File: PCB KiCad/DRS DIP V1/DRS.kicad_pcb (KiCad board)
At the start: 2 copper layers, 97.5 x 82.5 mm, 62 parts, among them J1 Jp7, J2 Jp8, J3 Jp8, J4 Conn_02x05_Odd_Even, SW1 SW_Push, SW2 SW_Push, SW3 SW_Push, U1 ATmega8-16PU, U2 LM2596S-ADJ, U3 LM2596S-ADJ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

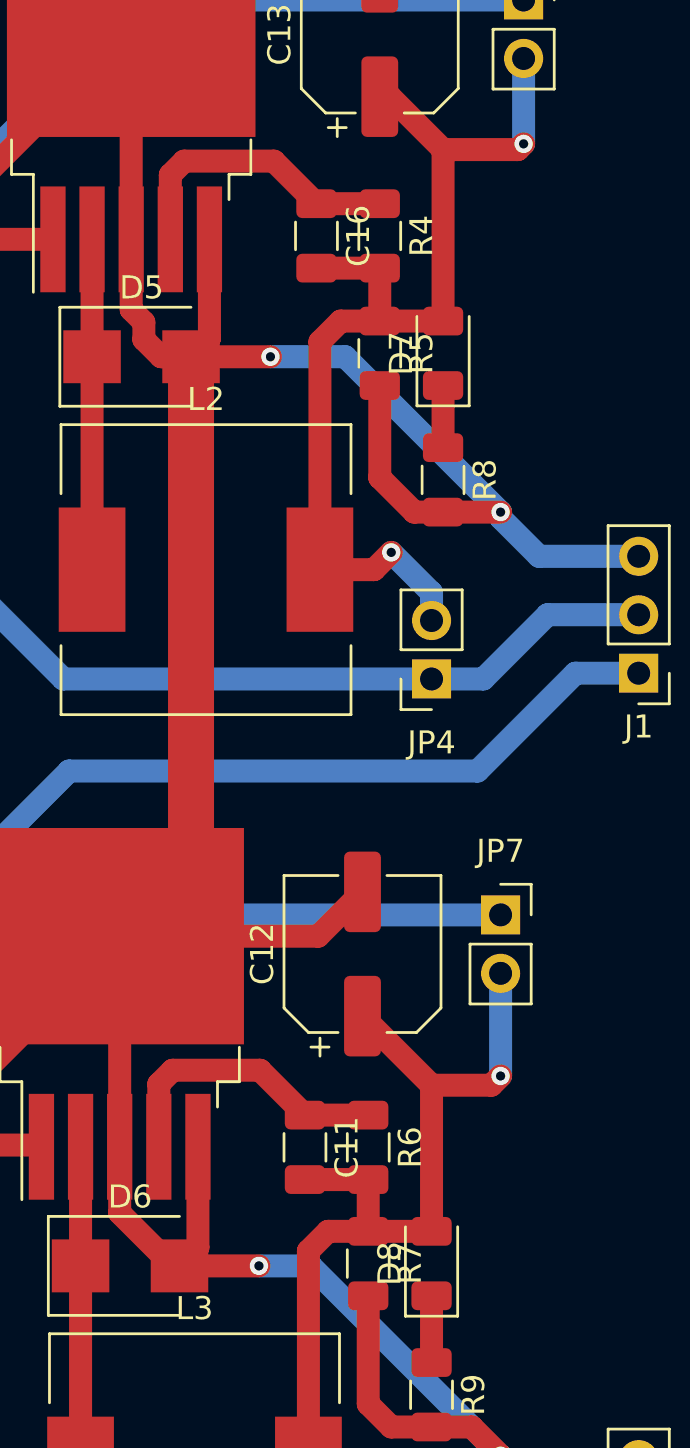
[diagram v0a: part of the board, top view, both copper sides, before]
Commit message: Adjustable voltage fix
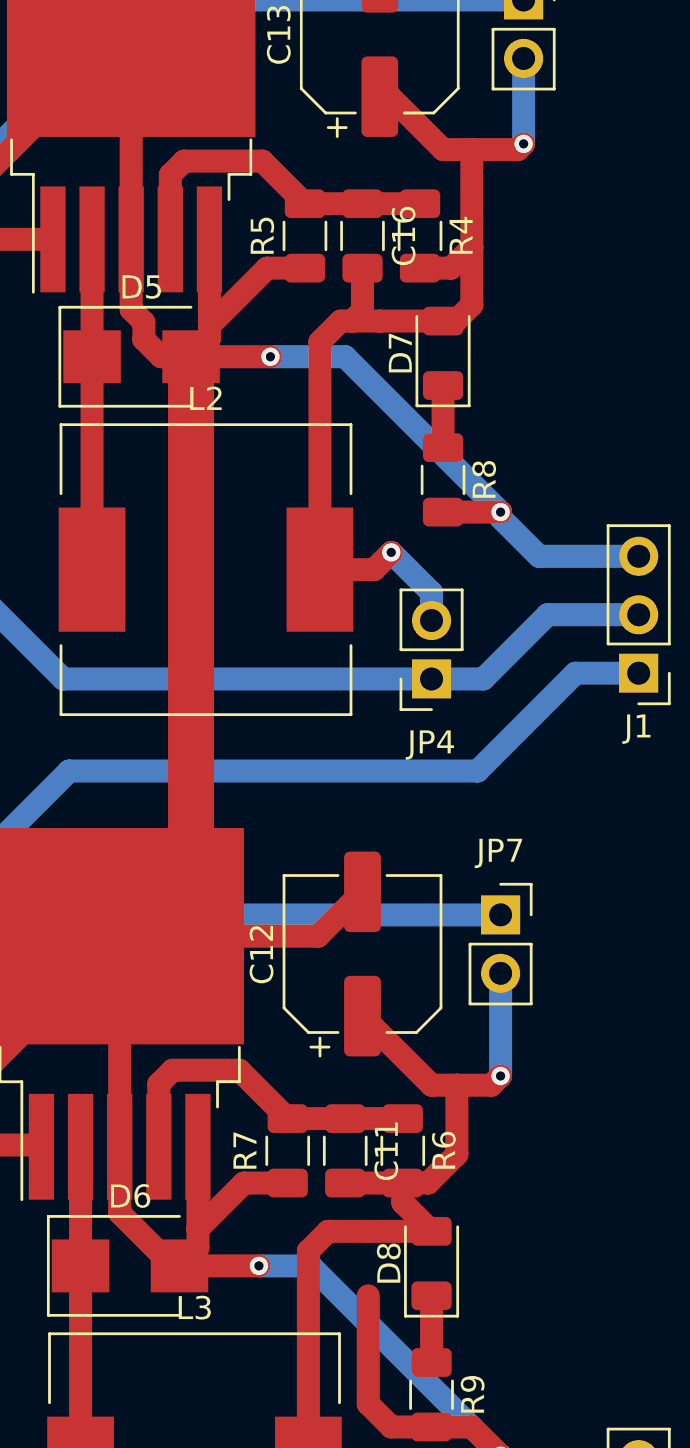
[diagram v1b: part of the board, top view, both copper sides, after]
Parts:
- moved R5 6.05 mm to (94.0, 46.5), turned to 90 degrees
- moved R7 6.02 mm to (93.2, 86.2), turned to 90 degrees
- moved C16 2.00 mm to (96.5, 46.5)
- moved C11 1.76 mm to (95.8, 86.2)
- moved R4 1.75 mm to (99.0, 46.5)
- moved R6 1.51 mm to (98.2, 86.2)
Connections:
- R5 pad 1: Net-(C13-Pad1) -> GND
- R5 pad 2: GND -> Net-(C16-Pad1)
- R7 pad 1: Net-(C11-Pad2) -> GND
- R7 pad 2: GND -> Net-(C11-Pad1)
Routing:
- net GND: track 358.1 -> 360.6 mm
- net Net-(C16-Pad1): track 12.9 -> 14.7 mm
- net Net-(C11-Pad1): track 12.9 -> 14.4 mm
- net Net-(C13-Pad1): track 46.2 -> 47.1 mm
